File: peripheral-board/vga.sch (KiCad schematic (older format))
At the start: 1 part, among them P9001 VGA

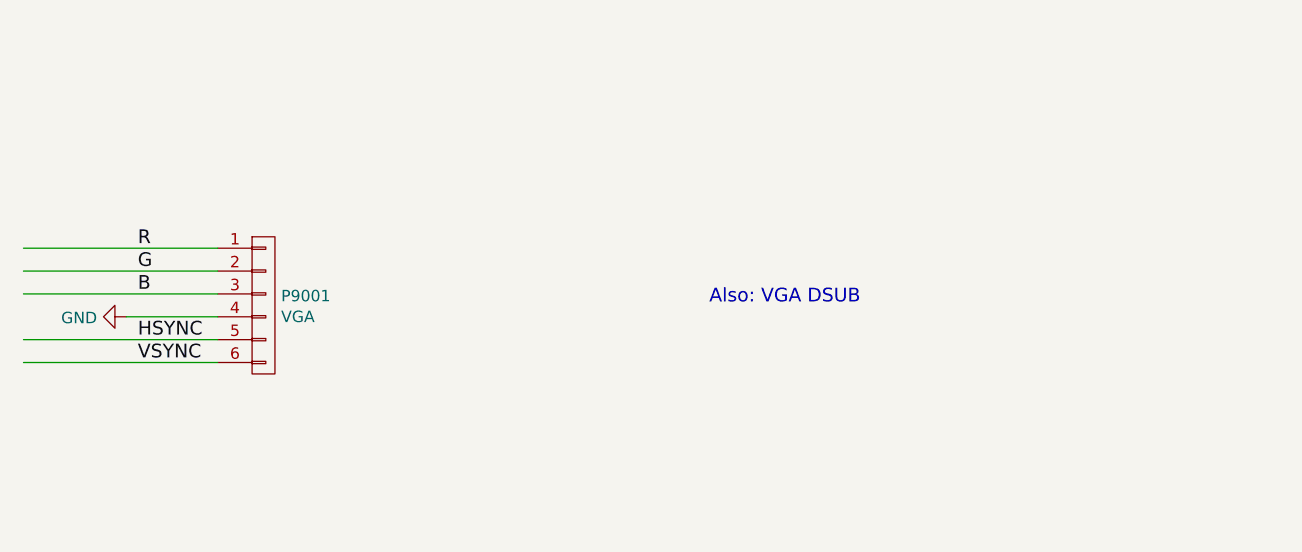
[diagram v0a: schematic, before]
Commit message: routed keyboard
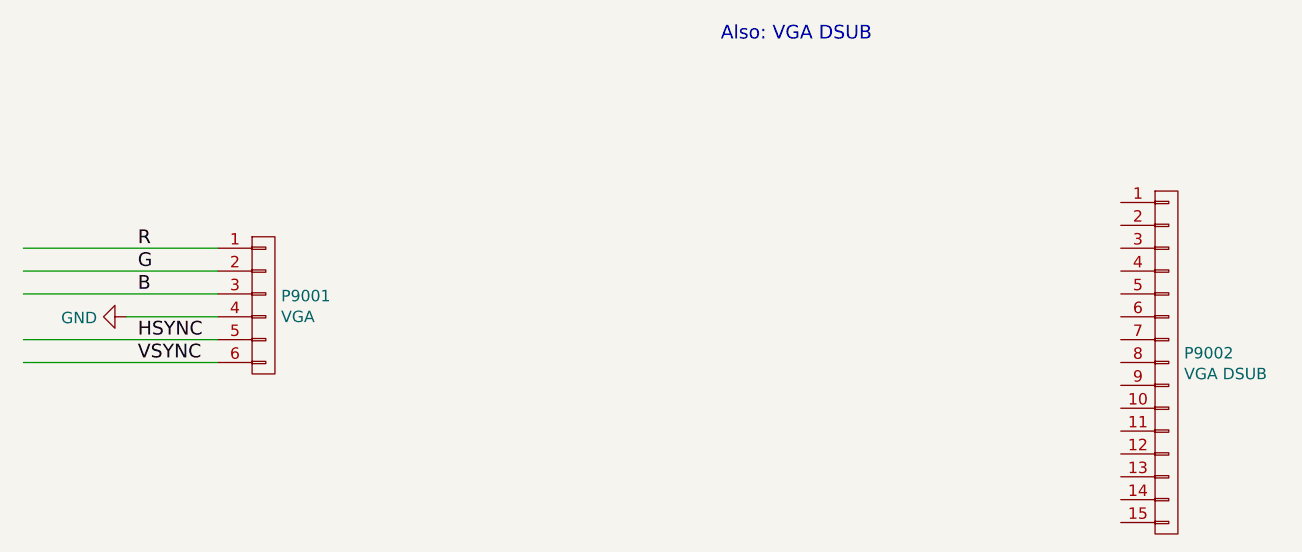
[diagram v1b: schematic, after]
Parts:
- added P9002: VGA DSUB, lib:HDDSUB-15-VGA, symbol CONN_01X15
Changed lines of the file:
@@
 LIBS:amp
 LIBS:card-edge
+LIBS:switchmode
+LIBS:joystick
 LIBS:peripheral-board-cache
 EELAYER 25 0
@@
 VSYNC
 $Comp
-L GND #PWR9001
+L GND #PWR035
 U 1 1 581F8A49
 P 4100 2450
-F 0 "#PWR9001" H 4100 2200 50  0001 C CNN
+F 0 "#PWR035" H 4100 2200 50  0001 C CNN
 F 1 "GND" V 4105 2322 50  0000 R CNN
 F 2 "" H 4100 2450 50  0000 C CNN
@@
 Wire Wire Line
 	4500 2450 4100 2450
-Text Notes 6650 2400 0    60   ~ 0
+Text Notes 6700 1250 0    60   ~ 0
 Also: VGA DSUB\n
+$Comp
+L CONN_01X15 P9002
+U 1 1 58220AA6
+P 8650 2650
+F 0 "P9002" H 8727 2691 50  0000 L CNN
+F 1 "VGA DSUB" H 8727 2600 50  0000 L CNN
+F 2 "lib:HDDSUB-15-VGA" H 8650 2650 50  0001 C CNN
+F 3 "" H 8650 2650 50  0000 C CNN
+	1    8650 2650
+	1    0    0    -1
+$EndComp
 $EndSCHEMATC

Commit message: added audio jack
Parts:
- removed P9002: VGA DSUB, lib:HDDSUB-15-VGA, symbol CONN_01X15
- added J10001: DB15_FEMALE_HighDensity, lib:HDDSUB-15-VGA, symbol DB15_FEMALE_HighDensity
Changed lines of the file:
@@
 $Descr A4 11693 8268
 encoding utf-8
-Sheet 9 10
+Sheet 10 10
 Title ""
 Date ""
@@
 VSYNC
 $Comp
-L GND #PWR041
+L GND #PWR067
 U 1 1 581F8A49
 P 4100 2450
-F 0 "#PWR041" H 4100 2200 50  0001 C CNN
+F 0 "#PWR067" H 4100 2200 50  0001 C CNN
 F 1 "GND" V 4105 2322 50  0000 R CNN
 F 2 "" H 4100 2450 50  0000 C CNN
@@
 Also: VGA DSUB\n
 $Comp
-L CONN_01X15 P9002
-U 1 1 58220AA6
-P 8650 2650
-F 0 "P9002" H 8727 2691 50  0000 L CNN
-F 1 "VGA DSUB" H 8727 2600 50  0000 L CNN
-F 2 "lib:HDDSUB-15-VGA" H 8650 2650 50  0001 C CNN
-F 3 "" H 8650 2650 50  0000 C CNN
-	1    8650 2650
+L DB15_FEMALE_HighDensity J10001
+U 1 1 589C4FB4
+P 7150 2650
+F 0 "J10001" H 7150 3517 50  0000 C CNN
+F 1 "DB15_FEMALE_HighDensity" H 7150 3426 50  0000 C CNN
+F 2 "lib:HDDSUB-15-VGA" H -1200 50  50  0001 C CNN
+F 3 "" H -1200 50  50  0001 C CNN
+	1    7150 2650
 	1    0    0    -1
 $EndComp

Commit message: audio circuitry
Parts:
- renumbered P9001 to P10001
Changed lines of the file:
@@
 EESchema Schematic File Version 2
+LIBS:peripheral-board-rescue
 LIBS:power
 LIBS:device
@@
 LIBS:digital-pot
 LIBS:vref
+LIBS:switches
 LIBS:peripheral-board-cache
 EELAYER 26 0
@@
 $EndDescr
 $Comp
-L CONN_01X06 P9001
+L CONN_01X06 P10001
 U 1 1 581F8990
 P 4700 2400
-F 0 "P9001" H 4777 2441 50  0000 L CNN
+F 0 "P10001" H 4777 2441 50  0000 L CNN
 F 1 "VGA" H 4777 2350 50  0000 L CNN
 F 2 "Socket_Strips:Socket_Strip_Straight_1x06" H 4700 2400 50  0001 C CNN
@@
 VSYNC
 $Comp
-L GND #PWR067
+L GND #PWR10001
 U 1 1 581F8A49
 P 4100 2450
-F 0 "#PWR067" H 4100 2200 50  0001 C CNN
+F 0 "#PWR10001" H 4100 2200 50  0001 C CNN
 F 1 "GND" V 4105 2322 50  0000 R CNN
 F 2 "" H 4100 2450 50  0000 C CNN

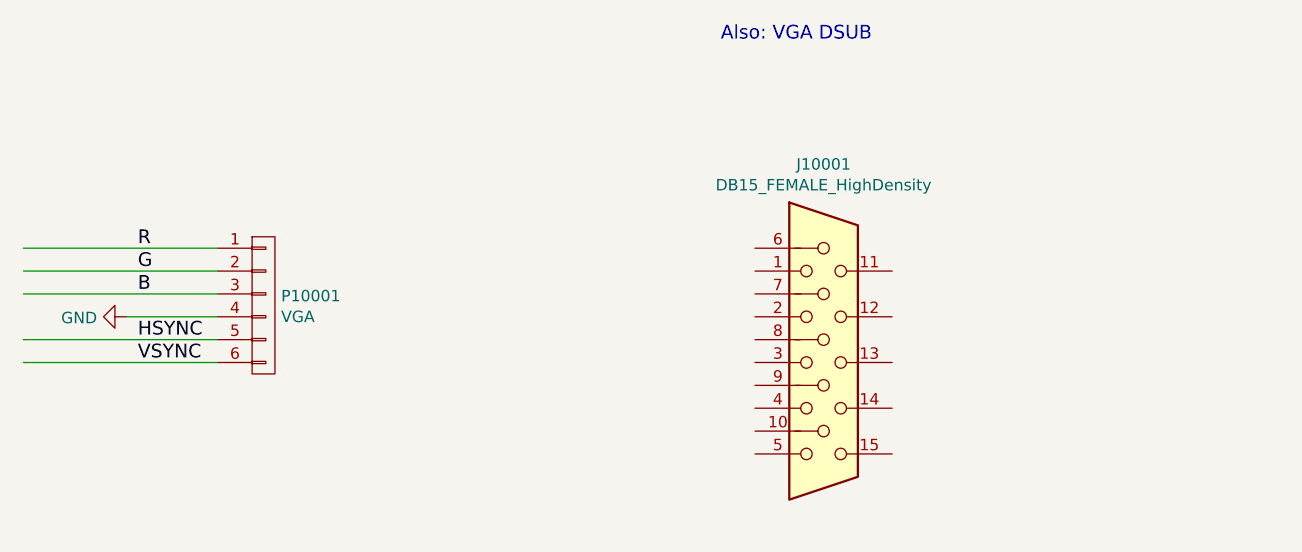
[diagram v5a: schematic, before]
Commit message: power supply component placement
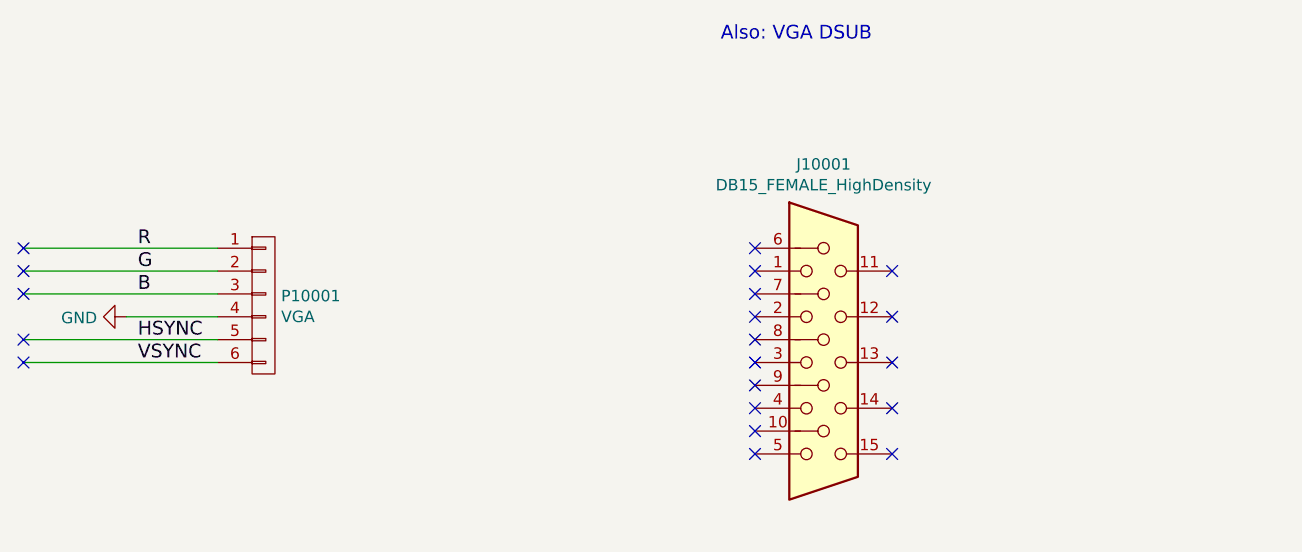
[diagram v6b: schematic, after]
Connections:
- no-connect marks 0 -> 20
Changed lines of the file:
@@
 	1    0    0    -1
 $EndComp
+NoConn ~ 3650 2150
+NoConn ~ 3650 2250
+NoConn ~ 3650 2350
+NoConn ~ 3650 2550
+NoConn ~ 3650 2650
+NoConn ~ 6850 2150
+NoConn ~ 6850 2250
+NoConn ~ 6850 2350
+NoConn ~ 6850 2450
+NoConn ~ 6850 2550
+NoConn ~ 6850 2650
+NoConn ~ 6850 2750
+NoConn ~ 6850 2850
+NoConn ~ 6850 2950
+NoConn ~ 6850 3050
+NoConn ~ 7450 2250
+NoConn ~ 7450 2450
+NoConn ~ 7450 2650
+NoConn ~ 7450 2850
+NoConn ~ 7450 3050
 $EndSCHEMATC
